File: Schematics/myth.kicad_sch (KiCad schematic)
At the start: 135 parts, among them J1 Conn_01x08_Male, J10 Conn_01x04_Male, J11 Conn_02x01, J2 Conn_01x08_Male, J3 Conn_01x08_Male, J4 Conn_01x08_Male, J5 Conn_01x08_Male, J6 Conn_01x08_Male, J8 Conn_01x08_Male, J9 Conn_01x04_Male, U1 74AHC02, U10 74HC595, U11 74HC165, U12 74AHC08, U13 74HC238, U14 74HC238, U15 74HC238, U16 4002, U17 74HC32, U18 74AHC273, U19 74LS32, U2 74AHC273, U20 CD4532BE, U21 74AHC138, U22 74AHC04, U23 74AHC138, U24 74HC238, U25 74HC238, U26 74LS32, U27 4078, U28 74AHC244, U29 74AHC138, U3 74HC74, U30 74AHC138, U31 4075, U32 74AHC02, U33 74AHC138, U34 74HC238, U35 74AHC138, U36 74HC163, U37 74AHC574, U38 74HC238, U39 74HC32, U4 74AHC04, U40 74AHC04, U41 74AHC574, U42 74HC74, U43 74AHC273, U44 74HC283, U45 74HC283, U46 74AHC273, U47 74HC02, U48 74HC157, U49 74HC157, U5 74AHC04, U50 74AHC244, U51 74AHC04, U52 74AHC574, U53 74HC193, U54 74HC193, U55 74HC193, U56 74HC193, U57 74HC193, U58 74HC193, U59 74HC193, U6 74AHC08, U60 74AHC244, U61 74LS32, U62 4078, U63 74AHC244, U64 74LS21, U65 74AHC04, U66 74AHC273, U67 74HC157, U68 74HC157, U69 74HC157, U7 74HC00, U70 74HC157, U71 74LS257, U72 74LS257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

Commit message: Fix names re. J, adjust opcodes and fix scrounger section in schematics
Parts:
- removed U44, U45: 74HC283, Package_DIP:DIP-16_W7.62mm_Socket_LongPads, symbol 74xx:74LS283
- added U44: 74LS08, symbol 74xx:74LS08
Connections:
- net +5V: now also U44.14 (VCC)
- net GND: now also U44.12, U44.13, U44.7 (GND)
- net Nx_pre: now also U44.1, U44.4
- net xL_pre: now also U44.2
- net xM_pre: now also U44.5
- net DEO: no longer names the net of U22.13, U27.3, U6.3
- net INO: no longer names the net of U27.2, U6.6
- net INO: no longer U7.1, U7.2
- net J0 renamed PC0
- net J1 renamed PC1
- net J2 renamed PC2
- net J3 renamed PC3
- net J4 renamed PC4
- net J5 renamed PC5
- net J6 renamed PC6
- net J7 renamed PC7
- net ORG renamed SIP
- net ~{DEO}: no longer names the net of U22.12, U8.12
- net ~{DEO}: no longer U57.4 (DOWN)
- net ~{INO} renamed ~{O1A}
- net ~{ORG} renamed ~{SIP}
- new net O1A: U44.3, U7.1, U7.2
- new net O1S: U44.10, U44.6, U44.9
- new net ~{O1S}: U44.8, U57.4 (DOWN)
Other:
- note added: "(PC Program Counter)"
- note added: "0000 => 0100 +4 R4A (R 4 ADD) 0001 +1 R1A 0010 +2 R2A 0011 +3 R3A 1100 -4 R4S (R 4 SUBTRACT) 1101 -3 R3S 1110 -2 R2S 1111 -1 R1S"
- note added: "NL => O1A (O 1 ADD) NM => O1S (O 1 SUBTRACT) LL => NOP (reserved) LM => NOP (reserved) ML => NOP (reserved) MM => NOP (reserved) GG => NOP (reserved) RR => NOP (reserved) II => NOP (reserved)"
- note removed: "(JUMP register) (Program Counter)"
- note removed: "(Relative addressing OPTIONAL! Feed RELx into U48/49 ==> instead of DBx)"
- note removed: "0000 => 0100 +4 P4 0001 +1 P1 0010 +2 P2 0011 +3 P3 1100 -4 M4 1101 -3 M3 1110 -2 M2 1111 -1 M1"
- note removed: "J"
- note removed: "NL => INO NM => DEO LL => NOP (reserved) LM => NOP (reserved) ML => NOP (reserved) MM => NOP (reserved) GG => NOP (reserved) RR => NOP (reserved) II => NOP (reserved)"
- note removed: "To do: Fix logic above to map NL to INO, and NM to DEO"
- moved on the sheet: U32A, U39A, U42B, U48, U49, U51F, U55, U56, U6D, U7A, U7D, U8A

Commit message: Add native division routine
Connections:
- net O1A renamed O1P
- net O1S renamed O1M
- net ~{O1A} renamed ~{O1P}
- net ~{O1S} renamed ~{O1M}
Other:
- note added: "0000 => 0100 +4 R4P (R 4 PLUS) 0001 +1 R1P 0010 +2 R2P 0011 +3 R3P 1100 -4 R4M (R 4 MINUS) 1101 -3 R3M 1110 -2 R2M 1111 -1 R1M"
- note added: "NL => O1P (O 1 PLUS) NM => O1M (O 1 MINUS) LL => NOP (reserved) LM => NOP (reserved) ML => NOP (reserved) MM => NOP (reserved) GG => NOP (reserved) RR => NOP (reserved) II => NOP (reserved)"
- note removed: "0000 => 0100 +4 R4A (R 4 ADD) 0001 +1 R1A 0010 +2 R2A 0011 +3 R3A 1100 -4 R4S (R 4 SUBTRACT) 1101 -3 R3S 1110 -2 R2S 1111 -1 R1S"
- note removed: "NL => O1A (O 1 ADD) NM => O1S (O 1 SUBTRACT) LL => NOP (reserved) LM => NOP (reserved) ML => NOP (reserved) MM => NOP (reserved) GG => NOP (reserved) RR => NOP (reserved) II => NOP (reserved)"
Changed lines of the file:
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@@
 		)
 	)
-	(text "                   NL => O1A (O 1 ADD)\n                   NM => O1S (O 1 SUBTRACT)\n                   LL => NOP (reserved)\n                   LM => NOP (reserved)\n                   ML => NOP (reserved)\n                   MM => NOP (reserved)\n                   GG => NOP (reserved)\n                   RR => NOP (reserved)\n                   II => NOP (reserved)"
+	(text "                   NL => O1P (O 1 PLUS)\n                   NM => O1M (O 1 MINUS)\n                   LL => NOP (reserved)\n                   LM => NOP (reserved)\n                   ML => NOP (reserved)\n                   MM => NOP (reserved)\n                   GG => NOP (reserved)\n                   RR => NOP (reserved)\n                   II => NOP (reserved)"
 		(exclude_from_sim no)
 		(at 194.3077 303.7819 0)
@@
 		)
 	)
-	(text "0000 => 0100  +4 R4A (R 4 ADD)\n        0001  +1 R1A\n        0010  +2 R2A\n        0011  +3 R3A\n        1100  -4 R4S (R 4 SUBTRACT)\n        1101  -3 R3S\n        1110  -2 R2S\n        1111  -1 R1S"
+	(text "0000 => 0100  +4 R4P (R 4 PLUS)\n        0001  +1 R1P\n        0010  +2 R2P\n        0011  +3 R3P\n        1100  -4 R4M (R 4 MINUS)\n        1101  -3 R3M\n        1110  -2 R2M\n        1111  -1 R1M"
 		(exclude_from_sim no)
 		(at 812.3355 186.0098 0)
@@
 		)
 	)
-	(label "O1S"
+	(label "O1M"
 		(at 246.1219 317.7599 0)
 		(fields_autoplaced yes)
@@
 		)
 	)
-	(label "~{O1A}"
+	(label "~{O1P}"
 		(at 887.6225 336.9828 180)
 		(fields_autoplaced yes)
@@
 		)
 	)
-	(label "~{O1A}"
+	(label "~{O1P}"
 		(at 741.2125 103.3523 0)
 		(fields_autoplaced yes)
@@
 		)
 	)
-	(label "O1A"
+	(label "O1P"
 		(at 247.1587 301.4313 0)
 		(fields_autoplaced yes)
@@
 		)
 	)
-	(label "~{O1S}"
+	(label "~{O1M}"
 		(at 712.206 103.1579 0)
 		(fields_autoplaced yes)
@@
 		)
 	)
-	(label "~{O1S}"
+	(label "~{O1M}"
 		(at 887.6225 339.5228 180)
 		(fields_autoplaced yes)
@@
 		)
 	)
-	(label "O1A"
+	(label "O1P"
 		(at 725.9725 100.8123 180)
 		(fields_autoplaced yes)
@@
 		)
 	)
-	(label "O1S"
+	(label "O1M"
 		(at 696.966 100.6179 180)
 		(fields_autoplaced yes)

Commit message: Implement changed semantics of xA in KiCad and myth[...].h
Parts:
- removed U44: 74LS08, symbol 74xx:74LS08
- removed U57, U95: 74HC193, Package_DIP:DIP-16_W7.62mm_Socket_LongPads, symbol 74xx:74LS193
- removed U73: 74AHC273, Package_DIP:DIP-20_W7.62mm_Socket_LongPads, symbol 74xx:74HC273
- removed U91, U92: 74HC283, Package_DIP:DIP-16_W7.62mm_Socket_LongPads, symbol 74xx:74LS283
- removed U93, U94: 74HC157, Package_DIP:DIP-16_W7.62mm_Socket_LongPads, symbol 74xx:74LS157
- added U44, U45: 74HC283, Package_DIP:DIP-16_W7.62mm_Socket_LongPads, symbol 74xx:74LS283
- added U57: 74AHC273, Package_DIP:DIP-20_W7.62mm_Socket_LongPads, symbol 74xx:74HC273
- added U74, U91: 74HC157, Package_DIP:DIP-16_W7.62mm_Socket_LongPads, symbol 74xx:74LS157
- added U92, U93: 74HC193, Package_DIP:DIP-16_W7.62mm_Socket_LongPads, symbol 74xx:74LS193
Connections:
- net GIN0 is gone; now on net DB0: U52.2 (D0)
- net GIN1 is gone; now on net DB1: U52.3 (D1)
- net GIN2 is gone; now on net DB2: U52.4 (D2)
- net GIN3 is gone; now on net DB3: U52.5 (D3)
- net GIN4 is gone; now on net DB4: U52.6 (D4)
- net GIN5 is gone; now on net DB5: U52.7 (D5)
- net GIN6 is gone; now on net DB6: U52.8 (D6)
- net GIN7 is gone; now on net DB7: U52.9 (D7)
- net +5V: now also U44.16 (VCC), U45.16 (VCC), U57.20 (VCC), U74.16 (VCC), U91.16 (VCC), U92.16 (VCC), U92.4 (DOWN), U93.16 (VCC)
- net D0: now also U92.3 (QA)
- net D1: now also U92.2 (QB)
- net D2: now also U92.6 (QC)
- net D3: now also U92.7 (QD)
- net D4: now also U93.3 (QA)
- net D5: now also U93.2 (QB)
- net D6: now also U93.6 (QC)
- net D7: now also U93.7 (QD)
- net DB0: now also U44.6 (B1), U91.2 (I0a); no longer U70.3 (I1a)
- net DB1: now also U44.2 (B2), U91.5 (I0b); no longer U70.6 (I1b)
- net DB2: now also U44.15 (B3), U91.11 (I0c); no longer U70.10 (I1c)
- net DB3: now also U44.11 (B4), U91.14 (I0d); no longer U70.13 (I1d)
- net DB4: now also U45.6 (B1), U74.2 (I0a); no longer U69.3 (I1a)
- net DB5: now also U45.2 (B2), U74.5 (I0b); no longer U69.6 (I1b)
- net DB6: now also U45.15 (B3), U74.11 (I0c); no longer U69.10 (I1c)
- net DB7: now also U45.11 (B4), U74.14 (I0d); no longer U69.13 (I1d)
- net GETO: now also U61.2; no longer U39.13
- net GND: now also U31.1, U31.2, U31.8, U44.7 (C0), U44.8 (GND), U45.8 (GND), U57.10 (GND), U74.15 (E), U74.8 (GND), U91.15 (E), U91.8 (GND), U92.8 (GND), U93.8 (GND); no longer U61.12, U61.13, U61.4, U61.5
- net O0: now also U57.2 (Q0)
- net O1: now also U57.5 (Q1)
- net O2: now also U57.6 (Q2)
- net O3: now also U57.9 (Q3)
- net O4: now also U57.12 (Q4)
- net O5: now also U57.15 (Q5)
- net O6: now also U57.16 (Q6)
- net O7: now also U57.19 (Q7)
- net RES: now also U92.14 (CLR), U93.14 (CLR)
- net SIP: now also U61.13; no longer U31.2
- net SUBR: now also U61.12; no longer U31.1
- net intoD: now also U1.9; no longer U31.8
- net xA: now also U61.1, U74.1 (S), U91.1 (S); no longer U61.2
- net xG: now also U26.1; no longer U61.1
- net ~{RES}: now also U57.1 (~{Mr})
- net at U39.11, U69.1 (S), U70.1 (S): now also U61.4; no longer U1.8
- net at U1.10: now also U92.11 (~{LOAD}), U93.11 (~{LOAD})
- net at U17.3: now also U61.5; no longer U1.9
- net at U68.12 (Zd): now also U93.9 (D)
- net at U68.4 (Za): now also U93.15 (A)
- net at U68.7 (Zb): now also U93.1 (B)
- net at U68.9 (Zc): now also U93.10 (C)
- net at U70.12 (Zd): now also U57.8 (D3)
- net at U70.4 (Za): now also U57.3 (D0)
- net at U70.7 (Zb): now also U57.4 (D1)
- net at U70.9 (Zc): now also U57.7 (D2)
- net at U69.12 (Zd): now also U57.18 (D7)
- net at U69.4 (Za): now also U57.13 (D4)
- net at U69.7 (Zb): now also U57.14 (D5)
- net at U69.9 (Zc): now also U57.17 (D6)
- net O2_post: now reaches U81.6 (Q2), U89.23 (A10)
- net O2_post: now also U44.14 (A3)
- net O3_post: now reaches U81.9 (Q3), U89.25 (A11)
- net O3_post: now also U44.12 (A4)
- net O1_post: now reaches U81.5 (Q1), U89.26 (A9)
- net O1_post: now also U44.3 (A2)
- net O0_post: now reaches U81.2 (Q0), U89.27 (A8)
- net O0_post: now also U44.5 (A1)
- net O5_post: now reaches U81.15 (Q5), U89.28 (A13)
- net O5_post: now also U45.3 (A2)
- net O6_post: now reaches U81.16 (Q6), U89.29 (A14)
- net O6_post: now also U45.14 (A3)
- net O7_post: now reaches U81.19 (Q7), U89.3 (A15)
- net O7_post: now also U45.12 (A4)
- net O4_post: now reaches U81.12 (Q4), U89.4 (A12)
- net O4_post: now also U45.5 (A1)
- net at U67.12 (Zd): now also U92.9 (D)
- net at U67.4 (Za): now also U92.15 (A)
- net at U67.7 (Zb): now also U92.1 (B)
- net at U67.9 (Zc): now also U92.10 (C)
- net at U61.6: now also U57.11 (Cp)
- net at U61.3: now also U39.13; no longer U26.1
- net at U61.11: now also U1.8
- net O1P: no longer names the net of U7.1, U7.2
- net O1P: now also U45.9 (C4)
- net ~{O1P}: no longer names the net of U7.3
- net ~{O1P}: now also U92.5 (UP)
- new net: U70.10 (I1c), U91.9 (Zc)
- new net: U70.13 (I1d), U91.12 (Zd)
- new net: U70.3 (I1a), U91.4 (Za)
- new net: U70.6 (I1b), U91.7 (Zb)
- new net: U45.1 (S2), U74.6 (I1b)
- new net: U45.10 (S4), U74.13 (I1d)
- new net: U45.13 (S3), U74.10 (I1c)
- new net: U45.4 (S1), U74.3 (I1a)
- new net: U44.9 (C4), U45.7 (C0)
- new net: U44.1 (S2), U91.6 (I1b)
- new net: U44.10 (S4), U91.13 (I1d)
- new net: U44.13 (S3), U91.10 (I1c)
- new net: U44.4 (S1), U91.3 (I1a)
- new net: U69.10 (I1c), U74.9 (Zc)
- new net: U69.13 (I1d), U74.12 (Zd)
- new net: U69.3 (I1a), U74.4 (Za)
- new net: U69.6 (I1b), U74.7 (Zb)
- new net ~{BOD}: U92.13 (~{BO}), U93.4 (DOWN)
- new net ~{COD}: U92.12 (~{CO}), U93.5 (UP)
- no-connect marks 66 -> 63
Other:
- note added: "Mapped to NOP, but reserved for instruction set extensions"
- note added: "Myth Microcontroller Reference Schematics Rev. LOX"
- note added: "NL => NOP (reserved) NM => NOP (reserved) LL => NOP (reserved) LM => NOP (reserved) ML => NOP (reserved) MM => NOP (reserved) GG => NOP (reserved) RR => NOP (reserved) II => NOP (reserved)"
- note added: "xA adds DB val to O and carries over into D"
- note removed: "Load DB value (xG) or DB + I (xA = "ADD")"
- note removed: "Most mapped to NOP, but reserved for instruction set extensions"
- note removed: "Myth Microcontroller Reference Schematics"
- note removed: "NL => O1P (O 1 PLUS) NM => O1M (O 1 MINUS) LL => NOP (reserved) LM => NOP (reserved) ML => NOP (reserved) MM => NOP (reserved) GG => NOP (reserved) RR => NOP (reserved) II => NOP (reserved)"
- moved on the sheet: U12A, U16B, U17A, U17B, U19A, U1C, U22A, U22B, U22C, U22D, U22E, U26A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

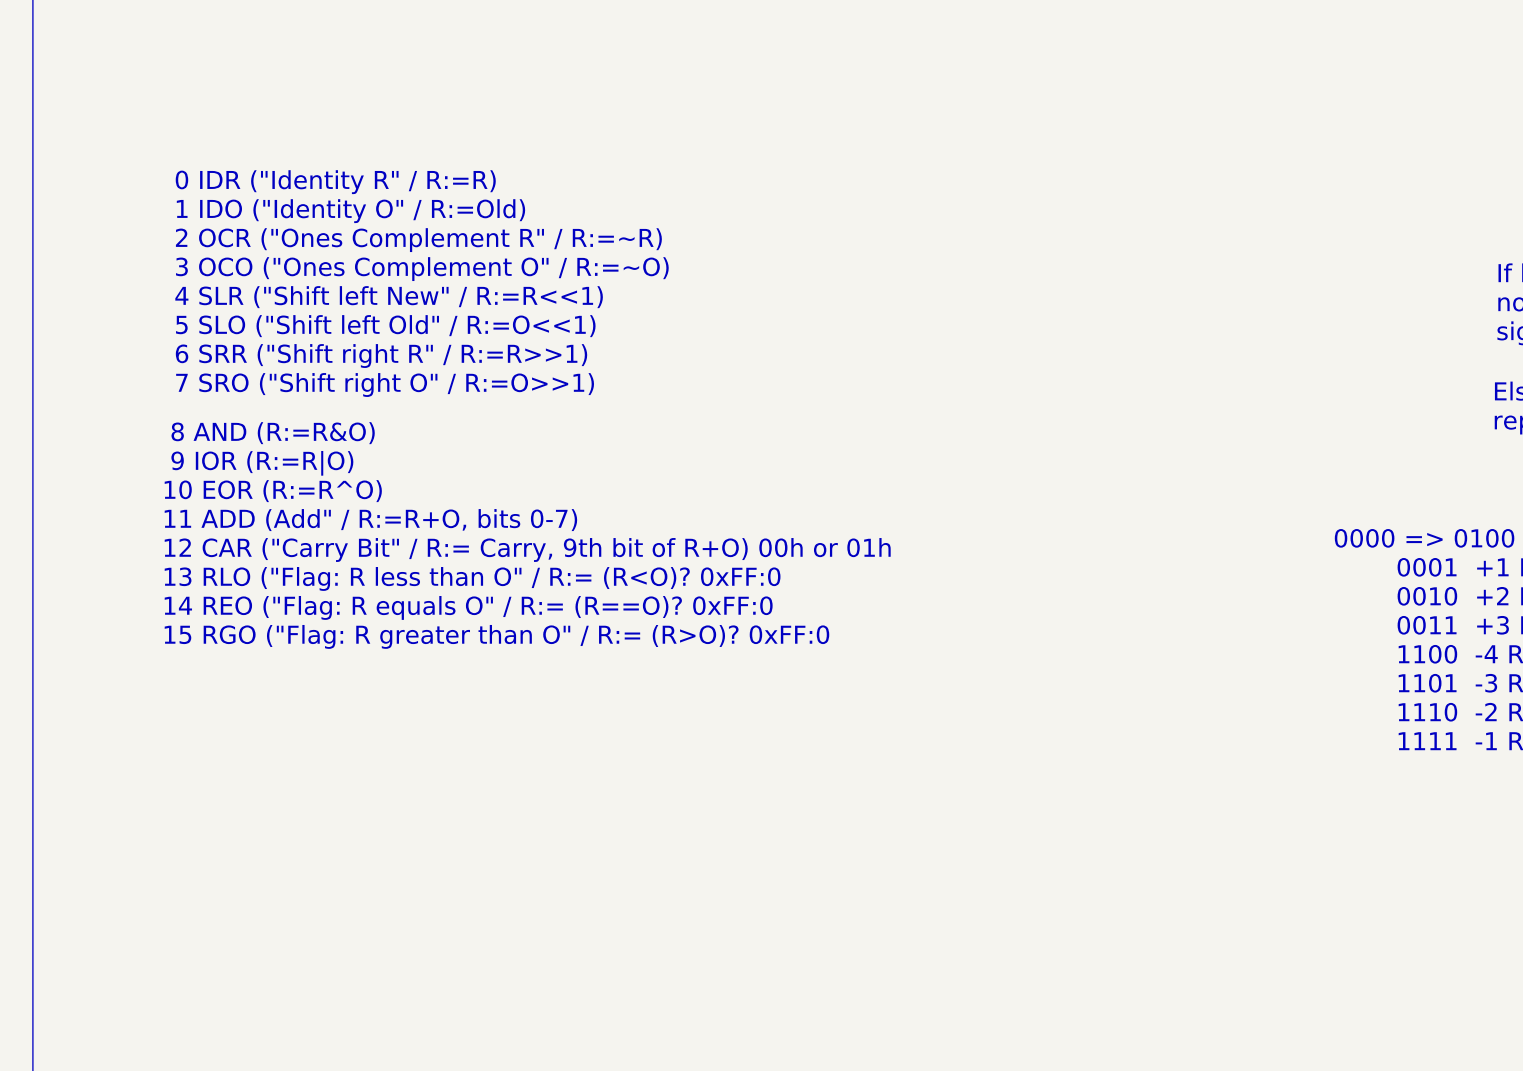
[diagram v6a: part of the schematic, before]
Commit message: Replace ALU opcode IDR with CLR (set R to zero)
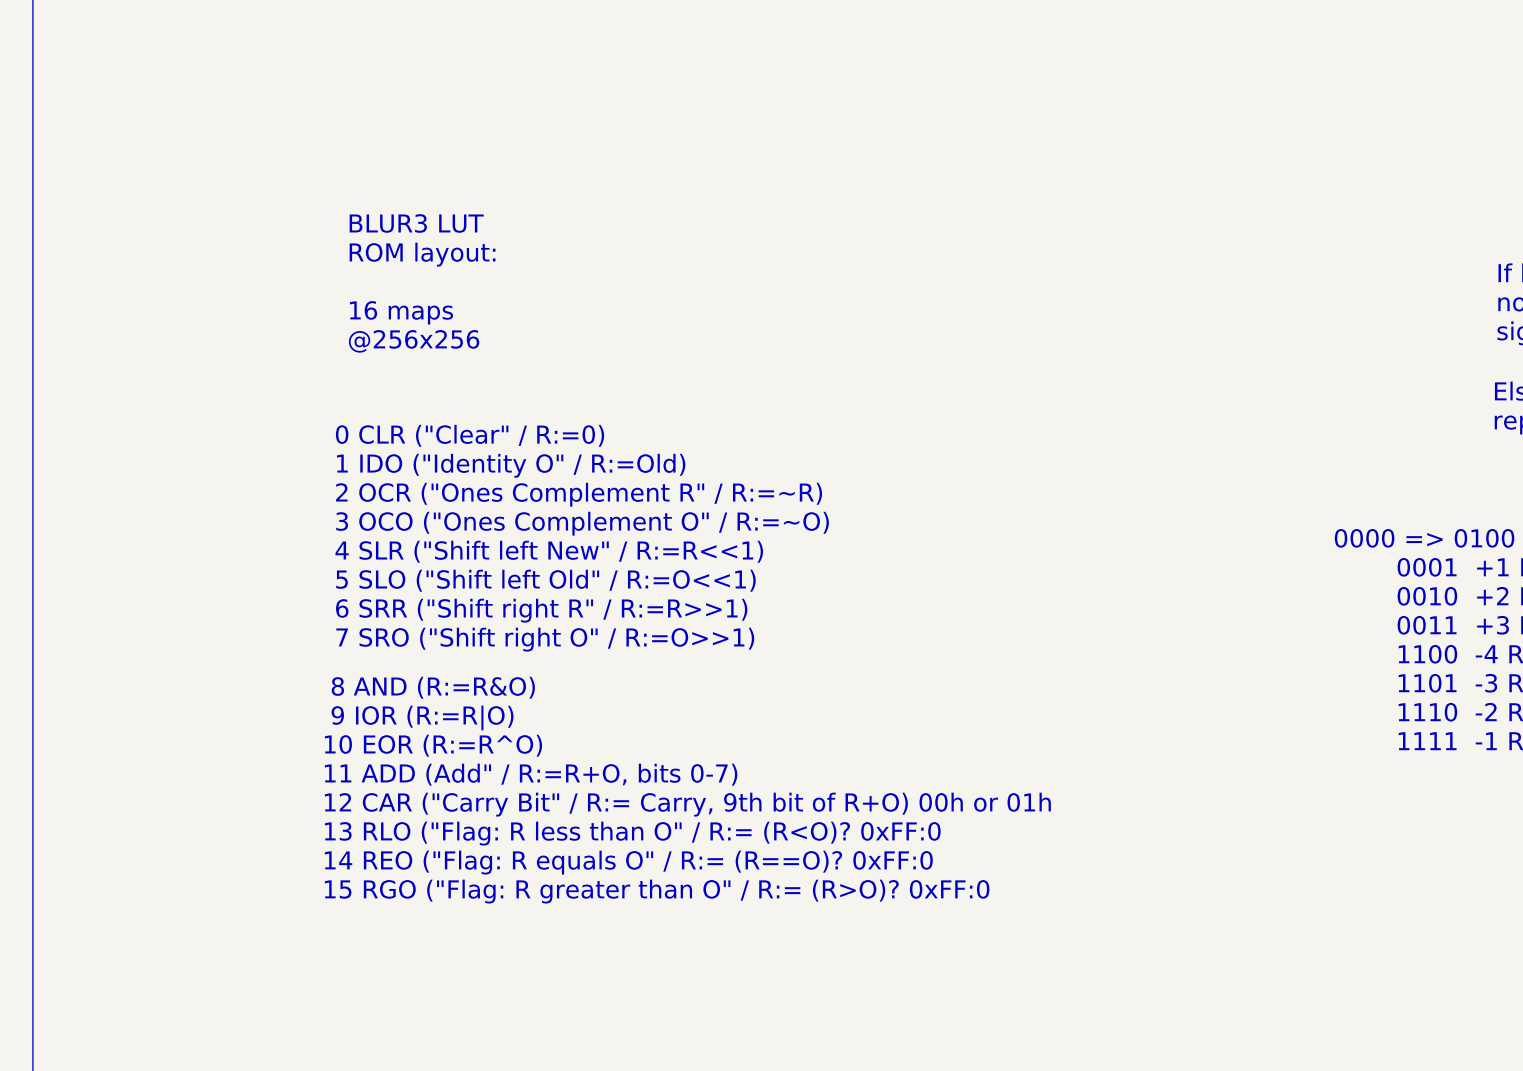
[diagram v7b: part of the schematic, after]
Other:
- note added: "0 CLR ("Clear" / R:=0) 1 IDO ("Identity O" / R:=Old) 2 OCR ("Ones Complement R" / R:=~R) 3 OCO ("Ones Complement O" / R:=~O) 4 SLR ("Shift left New" / R:=R<<1) 5 SLO ("Shift left Old" / R:=O<<1) 6 SRR ("Shift right R" / R:=R>>1) 7 SRO ("Shift right O" / R:=O>>1)"
- note removed: "0 IDR ("Identity R" / R:=R) 1 IDO ("Identity O" / R:=Old) 2 OCR ("Ones Complement R" / R:=~R) 3 OCO ("Ones Complement O" / R:=~O) 4 SLR ("Shift left New" / R:=R<<1) 5 SLO ("Shift left Old" / R:=O<<1) 6 SRR ("Shift right R" / R:=R>>1) 7 SRO ("Shift right O" / R:=O>>1)"
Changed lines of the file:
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@@
 		)
 	)
-	(text "0 IDR (\"Identity R\" / R:=R)\n1 IDO (\"Identity O\" / R:=Old)\n2 OCR (\"Ones Complement R\" / R:=~R)\n3 OCO (\"Ones Complement O\" / R:=~O)\n4 SLR (\"Shift left New\" / R:=R<<1)\n5 SLO (\"Shift left Old\" / R:=O<<1)\n6 SRR (\"Shift right R\" / R:=R>>1)\n7 SRO (\"Shift right O\" / R:=O>>1)"
-		(exclude_from_sim no)
-		(at 712.2724 142.3604 0)
+	(text "0 CLR (\"Clear\" / R:=0)\n1 IDO (\"Identity O\" / R:=Old)\n2 OCR (\"Ones Complement R\" / R:=~R)\n3 OCO (\"Ones Complement O\" / R:=~O)\n4 SLR (\"Shift left New\" / R:=R<<1)\n5 SLO (\"Shift left Old\" / R:=O<<1)\n6 SRR (\"Shift right R\" / R:=R>>1)\n7 SRO (\"Shift right O\" / R:=O>>1)"
+		(exclude_from_sim no)
+		(at 730.0706 170.6535 0)
 		(effects
 			(font
@@
 		)
 	)
+	(text "BLUR3 LUT\nROM layout:\n\n16 maps\n@256x256"
+		(exclude_from_sim no)
+		(at 731.5105 137.5351 0)
+		(effects
+			(font
+				(size 2 2)
+			)
+			(justify left bottom)
+		)
+	)
 	(text "~{RES} request"
 		(exclude_from_sim no)
@@
 	(text " 8 AND (R:=R&O)\n 9 IOR (R:=R|O)\n10 EOR (R:=R^O)\n11 ADD (Add\" / R:=R+O, bits 0-7)\n12 CAR (\"Carry Bit\" / R:= Carry, 9th bit of R+O) 00h or 01h\n13 RLO (\"Flag: R less than O\" / R:= (R<O)? 0xFF:0\n14 REO (\"Flag: R equals O\" / R:= (R==O)? 0xFF:0\n15 RGO (\"Flag: R greater than O\" / R:= (R>O)? 0xFF:0\n"
 		(exclude_from_sim no)
-		(at 710.9262 170.3512 0)
-		(effects
-			(font
+		(at 728.7244 198.6443 0)
+		(effects
+			(font

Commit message: Shorten ADJUST to FIX, rename FIX type opcodes
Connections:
- net opc_ADJUST renamed opc_FIX
- net ~{opc_ADJUST} renamed ~{opc_FIX}
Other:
- note added: "0000 => 0100 +4 P4 (R PLUS 4) 0001 +1 P1 0010 +2 P2 0011 +3 P3 1100 -4 M4 (R MINUS 4) 1101 -3 M3 1110 -2 M2 1111 -1 M1"
- note added: "ALU Instructions"
- note added: "Else sign extend bit 2"
- note added: "Hard-coded: if bits 0-2 all 0 replace by 4"
- note added: "Instruction byte: all0: OPC_SYS 00000 xxx See table @ SYS decoder else: OPC_FIX 00001 xxx b2:extended sign bit b1-0 LSB OPC_ALU 0001x xxx See table @ ALU OPC_TRAP 001xx xxx b4:MSB b3-0:LSB (remaining bits set 1) OPC_GETPUT 01xxx xxx b0-2 OFFS b3:GP B4-5:REG(RODG) OPC_PAIR 1xxxx xxx DEST SRC"
- note added: "R-Fix"
- note added: "Ref. implementation connects two independent 4-bit groups (high/low) to 4:16 decoders (for synchronised latch enable / output enable events of two devices)"
- note added: "Sonne-8 Microcontroller Reference Schematics Rev. Myth/LOX"
- note added: "W=While Intended to post decrement for either case"
- note removed: "0000 => 0100 +4 R4P (R 4 PLUS) 0001 +1 R1P 0010 +2 R2P 0011 +3 R3P 1100 -4 R4M (R 4 MINUS) 1101 -3 R3M 1110 -2 R2M 1111 -1 R1M"
- note removed: "Else hard-code replace 0 by 4"
- note removed: "If bits 0-2 not all zero, sign extend bit 2"
- note removed: "Instruction byte: all0: OPC_SYS 00000 xxx See table @ SYS decoder else: OPC_ADJUST 00001 xxx b2:extended sign bit b1-0 LSB OPC_ALU 0001x xxx See table @ ALU OPC_TRAP 001xx xxx b4:MSB b3-0:LSB (remaining bits set 1) OPC_GETPUT 01xxx xxx b0-2 OFFS b3:GP B4-5:REG(RODG) OPC_PAIR 1xxxx xxx DEST SRC"
- note removed: "Myth Microcontroller Reference Schematics Rev. LOX"
- note removed: "Ordinal 0 selects a NULL DEVICE Ref. implementation connects two independent 4-bit groups (high/low) to 4:16 encoders (for simultaneous latch enable / output enable of two separate devices)"
- note removed: "R Adjust"
- note removed: "W=While Intended to be post decrement"
- moved on the sheet: J1, J10, J11, J2, J3, J4, J5, J6, J8, J9, R2, U1B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
